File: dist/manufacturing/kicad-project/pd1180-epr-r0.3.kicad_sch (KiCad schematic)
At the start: 0 parts

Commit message: Implement dual USB power/data ECO and consolidate industrial I/O
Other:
- removed sheet USB and Motor Logic Supplies
- removed sheet USB-C EPR Power and USB Data
- added sheet PD and Motor Backup Supplies (logic_power.kicad_sch)
- added sheet USB DATA and Attach Sense (usb_data.kicad_sch)
- added sheet USB-C PD POWER (usb_pd.kicad_sch)
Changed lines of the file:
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@@
   (generator_version 0.0.1)
   (paper
-    A4
+    A3
   )
   (sheet_instances
@@
       (color 0 0 0 0)
     )
-    (property "Sheetname" "USB-C EPR Power and USB Data"
+    (property "Sheetname" "USB-C PD POWER"
       (id 0)
       (at 25.4 24.7 0)
@@
     (instances
       (project ""
-        (path "/93276a6d-ae71-49bc-84c0-d5988d306052"
+        (path "/c498c7fb-1599-494d-ace0-607a3ed08d67"
           (page "2")
         )
@@
       (color 0 0 0 0)
     )
-    (property "Sheetname" "USB and Motor Logic Supplies"
+    (property "Sheetname" "PD and Motor Backup Supplies"
       (id 0)
       (at 85.4 24.7 0)
@@
     (instances
       (project ""
-        (path "/93276a6d-ae71-49bc-84c0-d5988d306052"
+        (path "/c498c7fb-1599-494d-ace0-607a3ed08d67"
           (page "3")
         )
@@
     (instances
       (project ""
-        (path "/93276a6d-ae71-49bc-84c0-d5988d306052"
+        (path "/c498c7fb-1599-494d-ace0-607a3ed08d67"
           (page "4")
         )
@@
     (instances
       (project ""
-        (path "/93276a6d-ae71-49bc-84c0-d5988d306052"
+        (path "/c498c7fb-1599-494d-ace0-607a3ed08d67"
           (page "5")
         )
@@
     (instances
       (project ""
-        (path "/93276a6d-ae71-49bc-84c0-d5988d306052"
+        (path "/c498c7fb-1599-494d-ace0-607a3ed08d67"
           (page "6")
         )
@@
     (instances
       (project ""
-        (path "/93276a6d-ae71-49bc-84c0-d5988d306052"
+        (path "/c498c7fb-1599-494d-ace0-607a3ed08d67"
           (page "7")
         )
@@
     (instances
       (project ""
-        (path "/93276a6d-ae71-49bc-84c0-d5988d306052"
+        (path "/c498c7fb-1599-494d-ace0-607a3ed08d67"
           (page "8")
         )
@@
     (instances
       (project ""
-        (path "/93276a6d-ae71-49bc-84c0-d5988d306052"
+        (path "/c498c7fb-1599-494d-ace0-607a3ed08d67"
           (page "9")
         )
@@
     (instances
       (project ""
-        (path "/93276a6d-ae71-49bc-84c0-d5988d306052"
+        (path "/c498c7fb-1599-494d-ace0-607a3ed08d67"
           (page "10")
         )
@@
       (color 0 0 0 0)
     )
+    (property "Sheetname" "USB DATA and Attach Sense"
+      (id 0)
+      (at 85.4 134.70000000000002 0)
+      (effects
+        (font
+          (size 1.524 1.524)
+        )
+        (justify left bottom)
+      )
+    )
+    (property "Sheetfile" "usb_data.kicad_sch"
+      (id 1)
+      (at 85.4 161.1 0)
+      (effects
+        (font
+          (size 1.524 1.524)
+        )
+        (justify left top)
+      )
+    )
+    (instances
+      (project ""
+        (path "/c498c7fb-1599-494d-ace0-607a3ed08d67"
+          (page "11")
+        )
+      )
+    )
+  )
+  (sheet
+    (at 145.4 135.4)
+    (size 40 25)
+    (exclude_from_sim no)
+    (in_bom yes)
+    (on_board yes)
+    (dnp no)
+    (fields_autoplaced yes)
+    (stroke
+      (width 0.1524)
+      (type solid)
+    )
+    (fill
+      (color 0 0 0 0)
+    )
+    (property "Sheetname" "24 V Inputs and Step/Direction"
+      (id 0)
+      (at 145.4 134.70000000000002 0)
+      (effects
+        (font
+          (size 1.524 1.524)
+        )
+        (justify left bottom)
+      )
+    )
+    (property "Sheetfile" "inputs.kicad_sch"
+      (id 1)
+      (at 145.4 161.1 0)
+      (effects
+        (font
+          (size 1.524 1.524)
+        )
+        (justify left top)
+      )
+    )
+    (instances
+      (project ""
+        (path "/c498c7fb-1599-494d-ace0-607a3ed08d67"
+          (page "12")
+        )
+      )
+    )
+  )
+  (sheet
+    (at 205.4 135.4)
+    (size 40 25)
+    (exclude_from_sim no)
+    (in_bom yes)
+    (on_board yes)
+    (dnp no)
+    (fields_autoplaced yes)
+    (stroke
+      (width 0.1524)
+      (type solid)
+    )
+    (fill
+      (color 0 0 0 0)
+    )
     (property "Sheetname" "CAN, RS485 and RS232"
       (id 0)
-      (at 85.4 134.70000000000002 0)
+      (at 205.4 134.70000000000002 0)
       (effects
         (font
@@
     (property "Sheetfile" "serial.kicad_sch"
       (id 1)
-      (at 85.4 161.1 0)
-      (effects
-        (font
-          (size 1.524 1.524)
-        )
-        (justify left top)
-      )
-    )
-    (instances
-      (project ""
-        (path "/93276a6d-ae71-49bc-84c0-d5988d306052"
-          (page "11")
-        )
-      )
-    )
-  )
-  (sheet
-    (at 145.4 135.4)
-    (size 40 25)
-    (exclude_from_sim no)
-    (in_bom yes)
-    (on_board yes)
-    (dnp no)
-    (fields_autoplaced yes)
-    (stroke
-      (width 0.1524)
-      (type solid)
-    )
-    (fill
-      (color 0 0 0 0)
-    )
-    (property "Sheetname" "24 V Inputs and Step/Direction"
-      (id 0)
-      (at 145.4 134.70000000000002 0)
-      (effects
-        (font
-          (size 1.524 1.524)
-        )
-        (justify left bottom)
-      )
-    )
-    (property "Sheetfile" "inputs.kicad_sch"
-      (id 1)
-      (at 145.4 161.1 0)
-      (effects
-        (font
-          (size 1.524 1.524)
-        )
-        (justify left top)
-      )
-    )
-    (instances
-      (project ""
-        (path "/93276a6d-ae71-49bc-84c0-d5988d306052"
-          (page "12")
-        )
-      )
-    )
-  )
-  (sheet
-    (at 205.4 135.4)
+      (at 205.4 161.1 0)
+      (effects
+        (font
+          (size 1.524 1.524)
+        )
+        (justify left top)
+      )
+    )
+    (instances
+      (project ""
+        (path "/c498c7fb-1599-494d-ace0-607a3ed08d67"
+          (page "13")
+        )
+      )
+    )
+  )
+  (sheet
+    (at 25.4 190.4)
     (size 40 25)
     (exclude_from_sim no)
@@
     (property "Sheetname" "Hardware Enable and Outputs"
       (id 0)
-      (at 205.4 134.70000000000002 0)
+      (at 25.4 189.70000000000002 0)
       (effects
         (font
@@
     (property "Sheetfile" "outputs.kicad_sch"
       (id 1)
-      (at 205.4 161.1 0)
-      (effects
-        (font
-          (size 1.524 1.524)
-        )
-        (justify left top)
-      )
-    )
-    (instances
-      (project ""
-        (path "/93276a6d-ae71-49bc-84c0-d5988d306052"
-          (page "13")
-        )
-      )
+      (at 25.4 216.1 0)
+      (effects
+        (font
+          (size 1.524 1.524)
+        )
+        (justify left top)
+      )
+    )
+    (instances
+      (project ""
+        (path "/c498c7fb-1599-494d-ace0-607a3ed08d67"
+          (page "14")
+        )
+      )

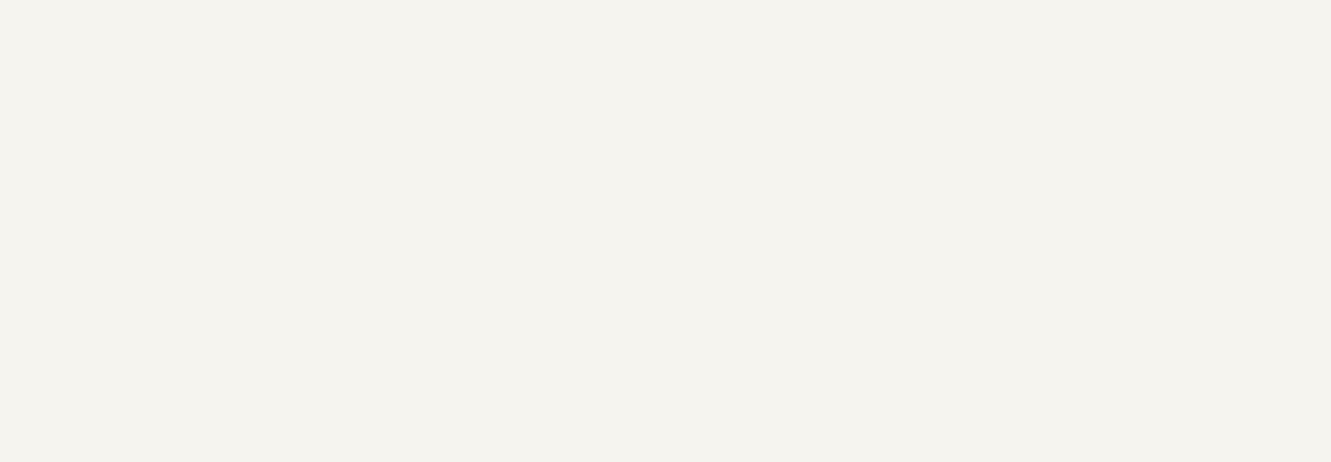
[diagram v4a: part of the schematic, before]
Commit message: Complete top-side routing and verify reference-board ECO
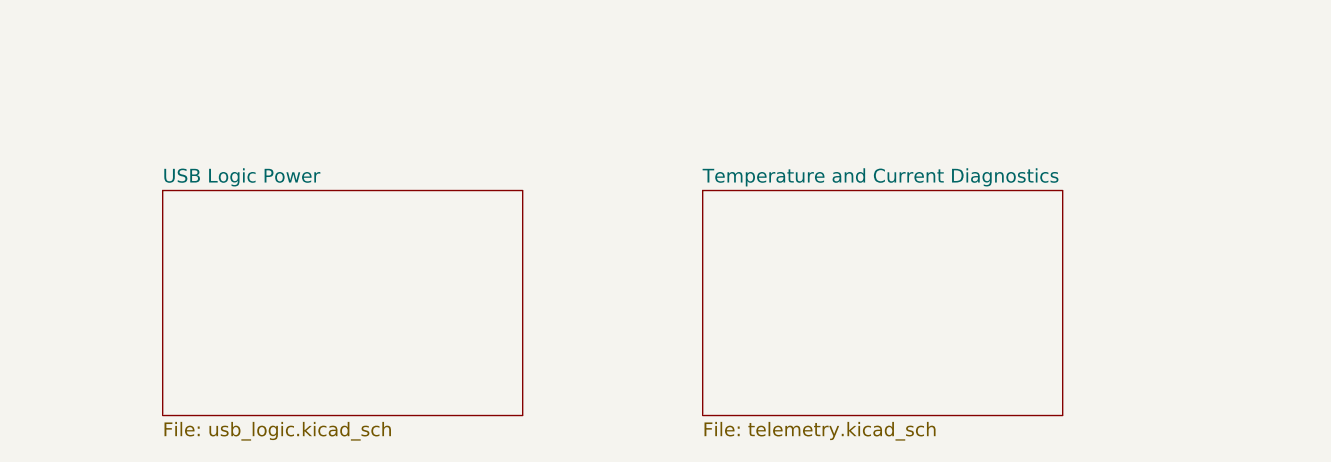
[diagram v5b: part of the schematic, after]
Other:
- added sheet Temperature and Current Diagnostics (telemetry.kicad_sch)
- added sheet USB Logic Power (usb_logic.kicad_sch)
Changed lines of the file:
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@@
     (instances
       (project ""
-        (path "/4ef2daa1-40fc-426a-abb2-c834ba40a3c9"
+        (path "/953e0ace-4c89-4879-a4e2-9aa73ffc3208"
           (page "2")
         )
@@
     (instances
       (project ""
-        (path "/4ef2daa1-40fc-426a-abb2-c834ba40a3c9"
+        (path "/953e0ace-4c89-4879-a4e2-9aa73ffc3208"
           (page "3")
         )
@@
     (instances
       (project ""
-        (path "/4ef2daa1-40fc-426a-abb2-c834ba40a3c9"
+        (path "/953e0ace-4c89-4879-a4e2-9aa73ffc3208"
           (page "4")
         )
@@
     (instances
       (project ""
-        (path "/4ef2daa1-40fc-426a-abb2-c834ba40a3c9"
+        (path "/953e0ace-4c89-4879-a4e2-9aa73ffc3208"
           (page "5")
         )
@@
     (instances
       (project ""
-        (path "/4ef2daa1-40fc-426a-abb2-c834ba40a3c9"
+        (path "/953e0ace-4c89-4879-a4e2-9aa73ffc3208"
           (page "6")
         )
@@
     (instances
       (project ""
-        (path "/4ef2daa1-40fc-426a-abb2-c834ba40a3c9"
+        (path "/953e0ace-4c89-4879-a4e2-9aa73ffc3208"
           (page "7")
         )
@@
     (instances
       (project ""
-        (path "/4ef2daa1-40fc-426a-abb2-c834ba40a3c9"
+        (path "/953e0ace-4c89-4879-a4e2-9aa73ffc3208"
           (page "8")
         )
@@
     (instances
       (project ""
-        (path "/4ef2daa1-40fc-426a-abb2-c834ba40a3c9"
+        (path "/953e0ace-4c89-4879-a4e2-9aa73ffc3208"
           (page "9")
         )
@@
     (instances
       (project ""
-        (path "/4ef2daa1-40fc-426a-abb2-c834ba40a3c9"
+        (path "/953e0ace-4c89-4879-a4e2-9aa73ffc3208"
           (page "10")
         )
@@
     (instances
       (project ""
-        (path "/4ef2daa1-40fc-426a-abb2-c834ba40a3c9"
+        (path "/953e0ace-4c89-4879-a4e2-9aa73ffc3208"
           (page "11")
         )
@@
     (instances
       (project ""
-        (path "/4ef2daa1-40fc-426a-abb2-c834ba40a3c9"
+        (path "/953e0ace-4c89-4879-a4e2-9aa73ffc3208"
           (page "12")
         )
@@
     (instances
       (project ""
-        (path "/4ef2daa1-40fc-426a-abb2-c834ba40a3c9"
+        (path "/953e0ace-4c89-4879-a4e2-9aa73ffc3208"
           (page "13")
         )
@@
     (instances
       (project ""
-        (path "/4ef2daa1-40fc-426a-abb2-c834ba40a3c9"
+        (path "/953e0ace-4c89-4879-a4e2-9aa73ffc3208"
           (page "14")
         )
       )
+    )
+  )
+  (sheet
+    (at 85.4 190.4)
+    (size 40 25)
+    (exclude_from_sim no)
+    (in_bom yes)
+    (on_board yes)
+    (dnp no)
+    (fields_autoplaced yes)
+    (stroke
+      (width 0.1524)
+      (type solid)
+    )
+    (fill
+      (color 0 0 0 0)
+    )
+    (property "Sheetname" "USB Logic Power"
+      (id 0)
+      (at 85.4 189.70000000000002 0)
+      (effects
+        (font
+          (size 1.524 1.524)
+        )
+        (justify left bottom)
+      )
+    )
+    (property "Sheetfile" "usb_logic.kicad_sch"
+      (id 1)
+      (at 85.4 216.1 0)
+      (effects
+        (font
+          (size 1.524 1.524)
+        )
+        (justify left top)
+      )
+    )
+    (instances
+      (project ""
+        (path "/953e0ace-4c89-4879-a4e2-9aa73ffc3208"
+          (page "15")
+        )
+      )
+    )
+  )
+  (sheet
+    (at 145.4 190.4)
+    (size 40 25)
+    (exclude_from_sim no)
+    (in_bom yes)
+    (on_board yes)
+    (dnp no)
+    (fields_autoplaced yes)
+    (stroke
+      (width 0.1524)
+      (type solid)
+    )
+    (fill
+      (color 0 0 0 0)
+    )
+    (property "Sheetname" "Temperature and Current Diagnostics"
+      (id 0)
+      (at 145.4 189.70000000000002 0)
+      (effects
+        (font
+          (size 1.524 1.524)
+        )
+        (justify left bottom)
+      )
+    )
+    (property "Sheetfile" "telemetry.kicad_sch"
+      (id 1)
+      (at 145.4 216.1 0)
+      (effects
+        (font
+          (size 1.524 1.524)
+        )
+        (justify left top)
+      )
+    )
+    (instances
+      (project ""
+        (path "/953e0ace-4c89-4879-a4e2-9aa73ffc3208"
+          (page "16")
+        )
+      )

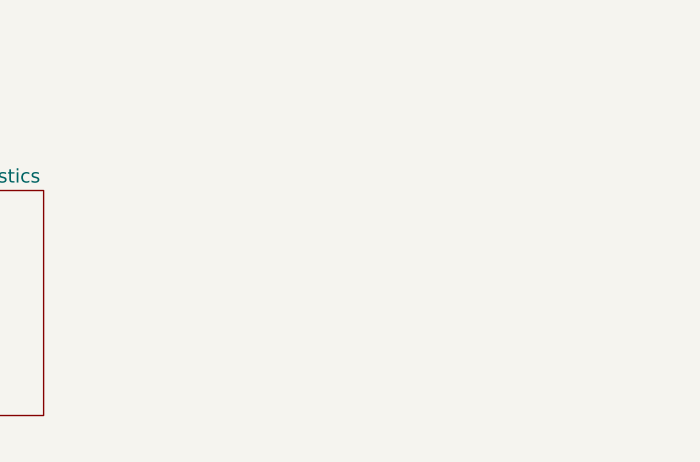
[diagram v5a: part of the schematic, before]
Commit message: Correct driver supply and brake protection power limits
Add the regulated 12 V TMC5160 gate supply and precision brake/OVP thresholds. Refresh top-side routing and manufacturing outputs with zero native DRC/ERC and complete connectivity. Verify native bypass paths and document calculations, sourcing, order holds, and unperformed powered tests.
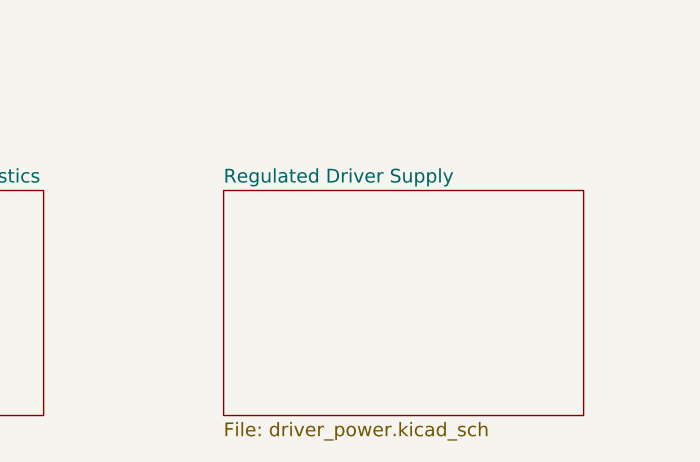
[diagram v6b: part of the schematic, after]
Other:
- added sheet Regulated Driver Supply (driver_power.kicad_sch)
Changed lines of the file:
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@@
     (instances
       (project ""
-        (path "/953e0ace-4c89-4879-a4e2-9aa73ffc3208"
+        (path "/c04facae-e812-4ae4-9853-e4e120a44c97"
           (page "2")
         )
@@
     (instances
       (project ""
-        (path "/953e0ace-4c89-4879-a4e2-9aa73ffc3208"
+        (path "/c04facae-e812-4ae4-9853-e4e120a44c97"
           (page "3")
         )
@@
     (instances
       (project ""
-        (path "/953e0ace-4c89-4879-a4e2-9aa73ffc3208"
+        (path "/c04facae-e812-4ae4-9853-e4e120a44c97"
           (page "4")
         )
@@
     (instances
       (project ""
-        (path "/953e0ace-4c89-4879-a4e2-9aa73ffc3208"
+        (path "/c04facae-e812-4ae4-9853-e4e120a44c97"
           (page "5")
         )
@@
     (instances
       (project ""
-        (path "/953e0ace-4c89-4879-a4e2-9aa73ffc3208"
+        (path "/c04facae-e812-4ae4-9853-e4e120a44c97"
           (page "6")
         )
@@
     (instances
       (project ""
-        (path "/953e0ace-4c89-4879-a4e2-9aa73ffc3208"
+        (path "/c04facae-e812-4ae4-9853-e4e120a44c97"
           (page "7")
         )
@@
     (instances
       (project ""
-        (path "/953e0ace-4c89-4879-a4e2-9aa73ffc3208"
+        (path "/c04facae-e812-4ae4-9853-e4e120a44c97"
           (page "8")
         )
@@
     (instances
       (project ""
-        (path "/953e0ace-4c89-4879-a4e2-9aa73ffc3208"
+        (path "/c04facae-e812-4ae4-9853-e4e120a44c97"
           (page "9")
         )
@@
     (instances
       (project ""
-        (path "/953e0ace-4c89-4879-a4e2-9aa73ffc3208"
+        (path "/c04facae-e812-4ae4-9853-e4e120a44c97"
           (page "10")
         )
@@
     (instances
       (project ""
-        (path "/953e0ace-4c89-4879-a4e2-9aa73ffc3208"
+        (path "/c04facae-e812-4ae4-9853-e4e120a44c97"
           (page "11")
         )
@@
     (instances
       (project ""
-        (path "/953e0ace-4c89-4879-a4e2-9aa73ffc3208"
+        (path "/c04facae-e812-4ae4-9853-e4e120a44c97"
           (page "12")
         )
@@
     (instances
       (project ""
-        (path "/953e0ace-4c89-4879-a4e2-9aa73ffc3208"
+        (path "/c04facae-e812-4ae4-9853-e4e120a44c97"
           (page "13")
         )
@@
     (instances
       (project ""
-        (path "/953e0ace-4c89-4879-a4e2-9aa73ffc3208"
+        (path "/c04facae-e812-4ae4-9853-e4e120a44c97"
           (page "14")
         )
@@
     (instances
       (project ""
-        (path "/953e0ace-4c89-4879-a4e2-9aa73ffc3208"
+        (path "/c04facae-e812-4ae4-9853-e4e120a44c97"
           (page "15")
         )
@@
     (instances
       (project ""
-        (path "/953e0ace-4c89-4879-a4e2-9aa73ffc3208"
+        (path "/c04facae-e812-4ae4-9853-e4e120a44c97"
           (page "16")
         )
       )
+    )
+  )
+  (sheet
+    (at 205.4 190.4)
+    (size 40 25)
+    (exclude_from_sim no)
+    (in_bom yes)
+    (on_board yes)
+    (dnp no)
+    (fields_autoplaced yes)
+    (stroke
+      (width 0.1524)
+      (type solid)
+    )
+    (fill
+      (color 0 0 0 0)
+    )
+    (property "Sheetname" "Regulated Driver Supply"
+      (id 0)
+      (at 205.4 189.70000000000002 0)
+      (effects
+        (font
+          (size 1.524 1.524)
+        )
+        (justify left bottom)
+      )
+    )
+    (property "Sheetfile" "driver_power.kicad_sch"
+      (id 1)
+      (at 205.4 216.1 0)
+      (effects
+        (font
+          (size 1.524 1.524)
+        )
+        (justify left top)
+      )
+    )
+    (instances
+      (project ""
+        (path "/c04facae-e812-4ae4-9853-e4e120a44c97"
+          (page "17")
+        )
+      )
